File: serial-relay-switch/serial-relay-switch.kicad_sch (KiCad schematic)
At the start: 78 parts, among them J1 Screw_Terminal_01x01, J10 Screw_Terminal_01x01, J11 Screw_Terminal_01x01, J17 Conn_01x01, J18 Conn_01x01, J19 Screw_Terminal_01x01, J2 2501551-4, J20 Screw_Terminal_01x01, J21 Conn_01x01, J4 Screw_Terminal_01x01, J5 Screw_Terminal_01x01, J6 Screw_Terminal_01x01, J7 Screw_Terminal_01x01, J8 Screw_Terminal_01x01, J9 Screw_Terminal_01x01, K1 G2RL-1-E, K2 G2RL-1-E, K3 G2RL-1-E, K4 G2RL-1-E, K5 G2RL-1-E, K6 G2RL-1-E, K7 G2RL-1-E, K8 G2RL-1-E, U1 H11L1, U10 SZNUD3124LT1G, U11 SZNUD3124LT1G, U12 SZNUD3124LT1G, U13 74HCT595, U14 74LVC1G32, U15 74LVC1G08, U16 74LVC1G04, U17 74LS163, U2 ISL8488E, U3 SZNUD3124LT1G, U4 ISL8488E, U6 SZNUD3124LT1G, U7 SZNUD3124LT1G, U8 SZNUD3124LT1G, U9 SZNUD3124LT1G

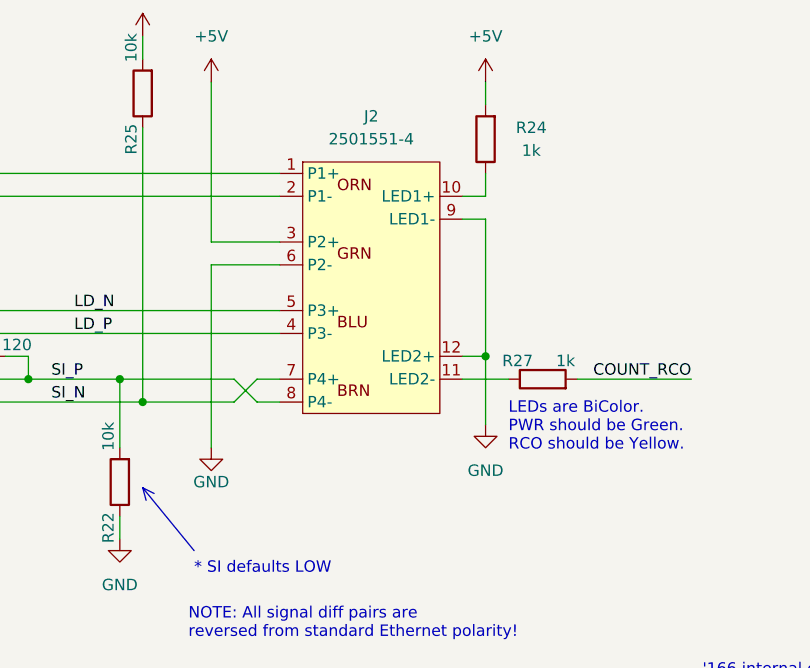
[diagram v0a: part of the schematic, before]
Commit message: [rs] Add RJ-45 shield connection; Export v1.0A1 gerbers
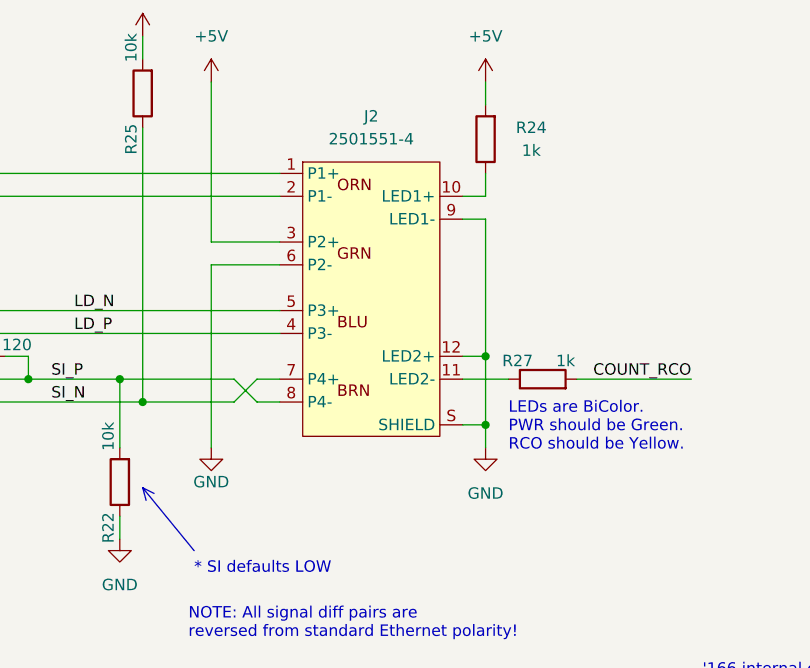
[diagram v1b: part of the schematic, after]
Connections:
- net GND: now also J2.S (SHIELD)
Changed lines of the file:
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@@
 	)
 	(junction
+		(at 142.24 226.06)
+		(diameter 0)
+		(color 0 0 0 0)
+	)
+	(junction
 		(at 167.64 40.64)
 		(diameter 0)
@@
 	)
 	(junction
-		(at 142.24 226.06)
-		(diameter 0)
-		(color 0 0 0 0)
-	)
-	(junction
 		(at 45.72 139.7)
 		(diameter 0)
@@
 	)
 	(junction
+		(at 142.24 233.68)
+		(diameter 0)
+		(color 0 0 0 0)
+	)
+	(junction
 		(at 276.86 53.34)
 		(diameter 0)
@@
 	(wire
 		(pts
+			(xy 142.24 233.68) (xy 142.24 236.22)
+		)
+		(stroke
+			(width 0)
+			(type default)
+		)
+	)
+	(wire
+		(pts
 			(xy 353.06 106.68) (xy 355.6 106.68)
 		)
@@
 	(wire
 		(pts
+			(xy 139.7 233.68) (xy 142.24 233.68)
+		)
+		(stroke
+			(width 0)
+			(type default)
+		)
+	)
+	(wire
+		(pts
 			(xy 33.02 20.32) (xy 33.02 33.02)
 		)
@@
 	(symbol
 		(lib_id "power:GND")
-		(at 142.24 233.68 0)
+		(at 142.24 236.22 0)
 		(unit 1)
 		(body_style 1)
@@
 		(fields_autoplaced yes)
 		(property "Reference" "#PWR025"
-			(at 142.24 240.03 0)
+			(at 142.24 242.57 0)
 			(hide yes)
 			(show_name no)
@@
 		)
 		(property "Value" "GND"
-			(at 142.24 238.76 0)
+			(at 142.24 241.3 0)
 			(show_name no)
 			(do_not_autoplace no)
@@
 		)
 		(property "Footprint" ""
-			(at 142.24 233.68 0)
+			(at 142.24 236.22 0)
 			(hide yes)
 			(show_name no)
@@
 		)
 		(property "Datasheet" ""
-			(at 142.24 233.68 0)
+			(at 142.24 236.22 0)
 			(hide yes)
 			(show_name no)
@@
 		)
 		(property "Description" "Power symbol creates a global label with name \"GND\" , ground"
-			(at 142.24 233.68 0)
+			(at 142.24 236.22 0)
 			(hide yes)
 			(show_name no)
@@
 		(pin "3"
 		)
+		(pin "S"
+		)
 		(instances

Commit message: [rs] Add PoR; Change to SC-74 coil driver package
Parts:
- removed U10, U11, U12, U3, U6, U7, U8, U9: SZNUD3124LT1G, Package_TO_SOT_SMD:SOT-23, symbol CUSTOM:SZNUD3124LT1G
- removed U13: 74HCT595, Package_SO:SOIC-16_3.9x9.9mm_P1.27mm, symbol 74xx:74HCT595
- added U13: STM1810T, Package_TO_SOT_SMD:SOT-23-3, symbol CUSTOM:STM1818T
- added U3, U6, U7, U8: SZNUD3124DMT1G, Package_TO_SOT_SMD:SC-74-6_1.55x2.9mm_P0.95mm, symbol CUSTOM:SZNUD3124DMT1G
- added U5: 74HC594, Package_SO:SOIC-16_3.9x9.9mm_P1.27mm, symbol 74xx:74HC594
- H1, H2: footprint CUSTOM:MountingHole_3.2mm_M3 -> CUSTOM:MountingHole_3.2mm_M3_Keepout
- J1, J10, J11, J19, J20, J4, J5, J6, J7, J8, J9: footprint CUSTOM:8195 -> CUSTOM:ScrewTerminal_Keystone_8195
- J2: footprint CUSTOM:2501551-4 -> CUSTOM:EthernetJack_TE_2501551-4
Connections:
- net +5V: now also U13.2 (VCC), U5.10 (~{SRCLR}), U5.16 (VCC)
- net CTL_A: now also U3.2, U5.15 (QA)
- net CTL_B: now also U3.5, U5.1 (QB)
- net CTL_C: now also U5.2 (QC), U6.2
- net CTL_D: now also U5.3 (QD), U6.5
- net CTL_E: now also U5.4 (QE), U7.2
- net CTL_F: now also U5.5 (QF), U7.5
- net CTL_G: now also U5.6 (QG), U8.2
- net CTL_H: now also U5.7 (QH), U8.5
- net GND: now also U13.3 (GND), U3.1, U3.4, U5.8 (GND), U6.1, U6.4, U7.1, U7.4, U8.1, U8.4
- net OUTPUT_UPDATE: now also U5.12 (RCLK)
- net RECEIVE_CLK: now also U5.11 (SRCLK)
- net SCAN_IN: now also U5.14 (SER)
- net at K6.A2: now also U7.3
- net at K7.A2: now also U8.6
- net at K4.A2: now also U3.3
- net at K2.A2: now also U6.6
- net at K3.A2: now also U7.6
- net at K1.A2: now also U3.6
- net at K5.A2: now also U6.3
- net at K8.A2: now also U8.3
- new net: U13.1 (RST), U5.13 (~{RCLR})
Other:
- moved on the sheet: D2, D3, D4, D5, D6, D7, D8, D9, R1, R2, R3, R4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

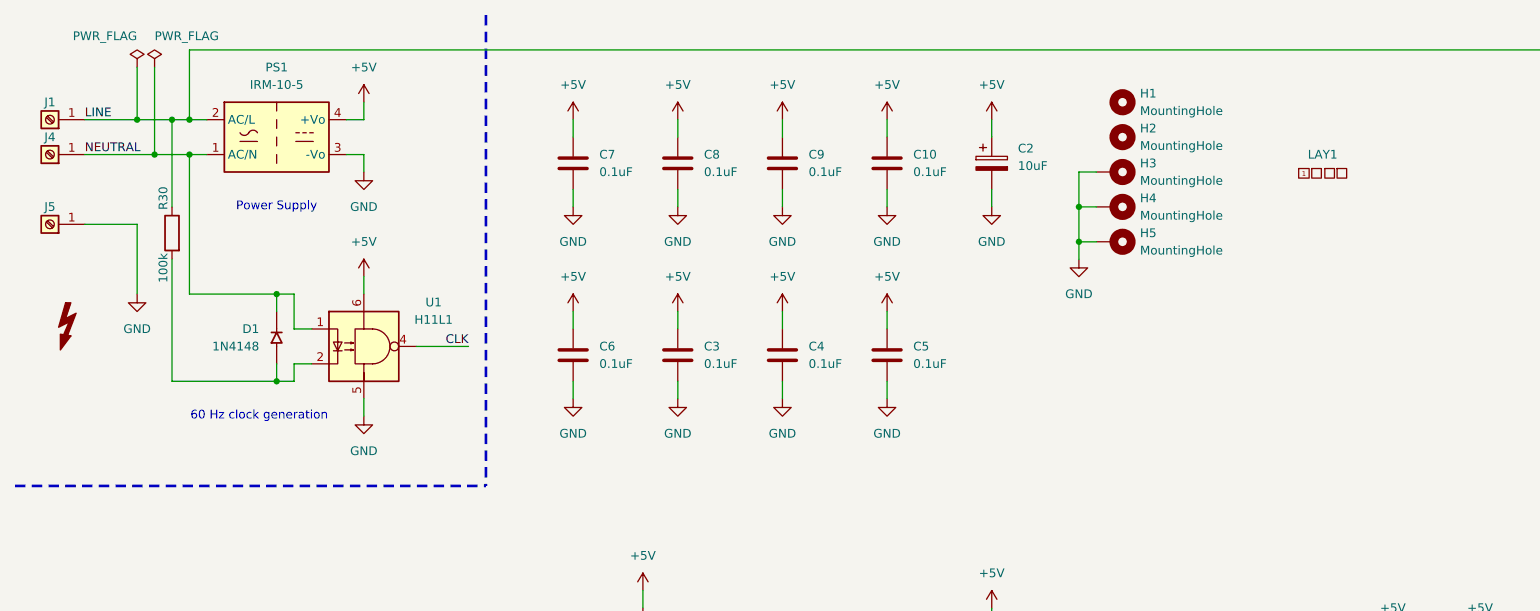
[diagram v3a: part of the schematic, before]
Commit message: [rs] Add missing pullup on CLK; bump to v1.1A
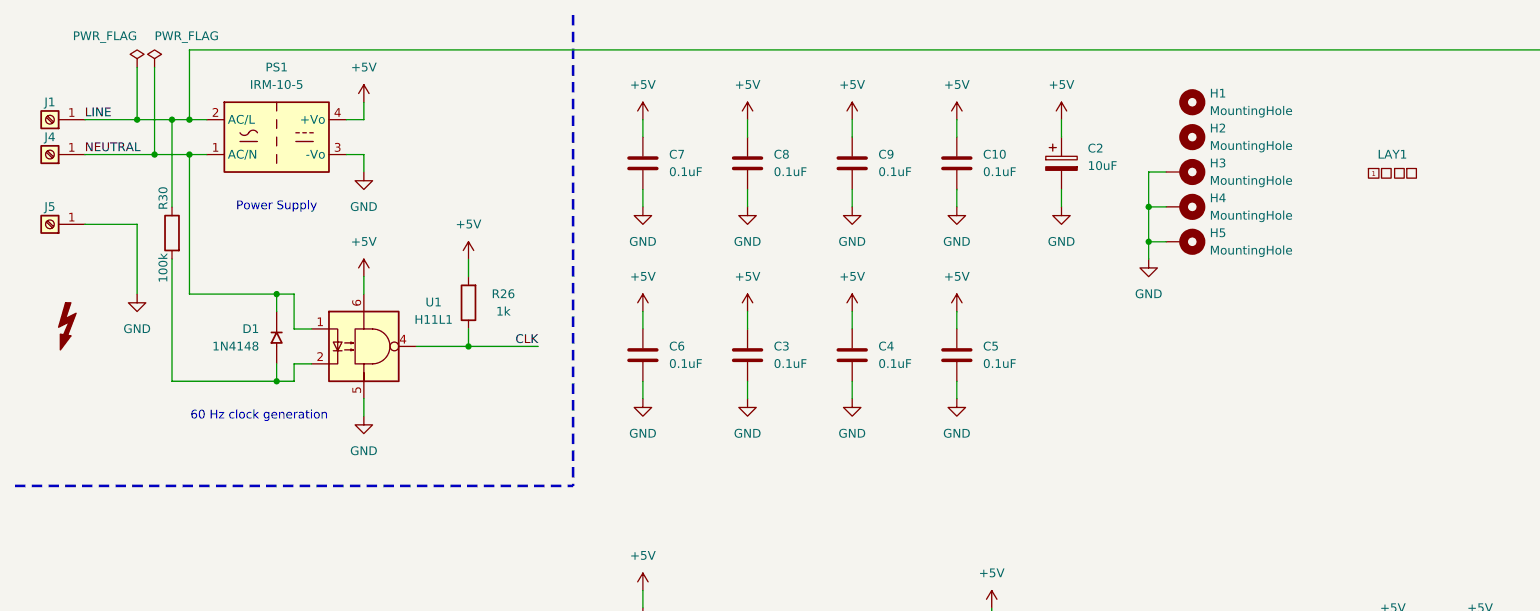
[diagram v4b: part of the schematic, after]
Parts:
- added R26: 1k, Resistor_SMD:R_0603_1608Metric, symbol CUSTOM:R
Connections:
- net +5V: now also R26.2
- net CLK: now also R26.1
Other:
- moved on the sheet: C10, C2, C3, C4, C5, C6, C7, C8, C9, H1, H2, H3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
